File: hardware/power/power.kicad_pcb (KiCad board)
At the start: 2 copper layers, 74 x 34 mm, 18 parts, among them J1 Screw_Terminal_01x02, J2 Screw_Terminal_01x03, Q1 BSS123, U1 AL8861

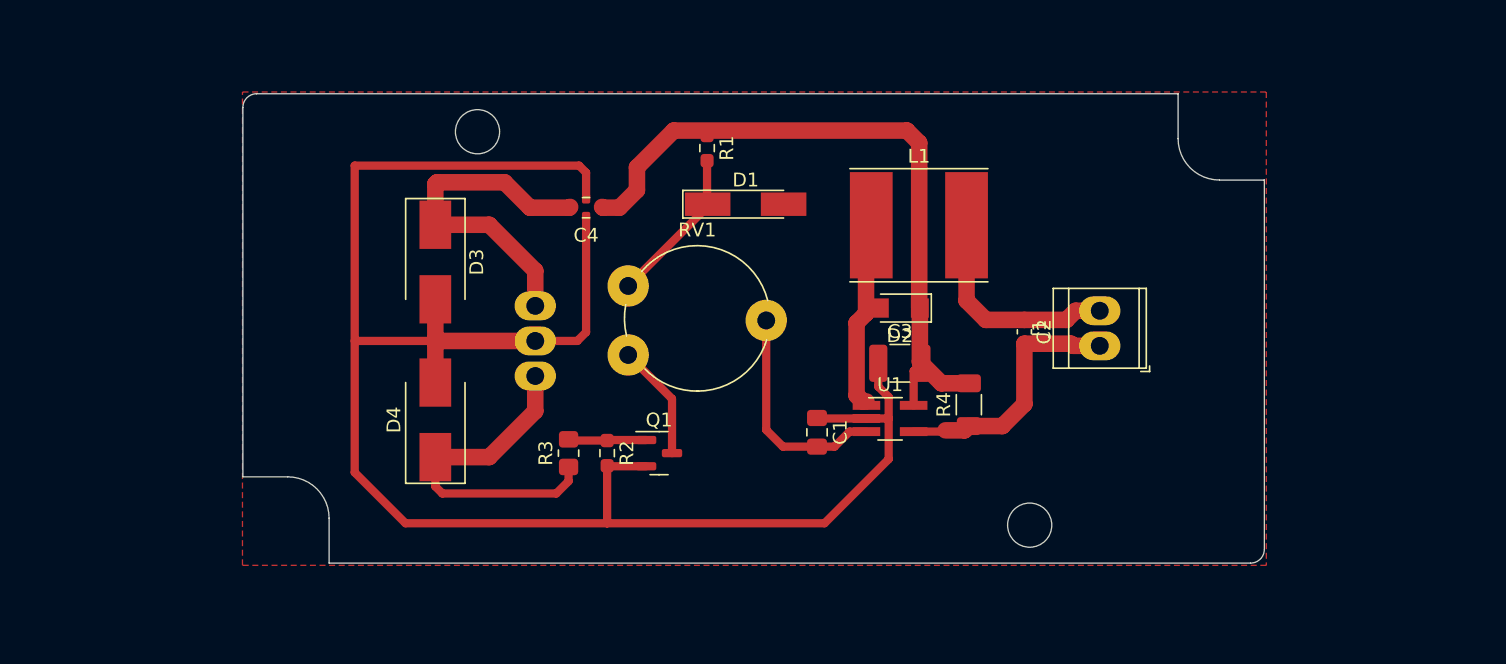
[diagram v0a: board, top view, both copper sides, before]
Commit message: change connectors for SMD ones
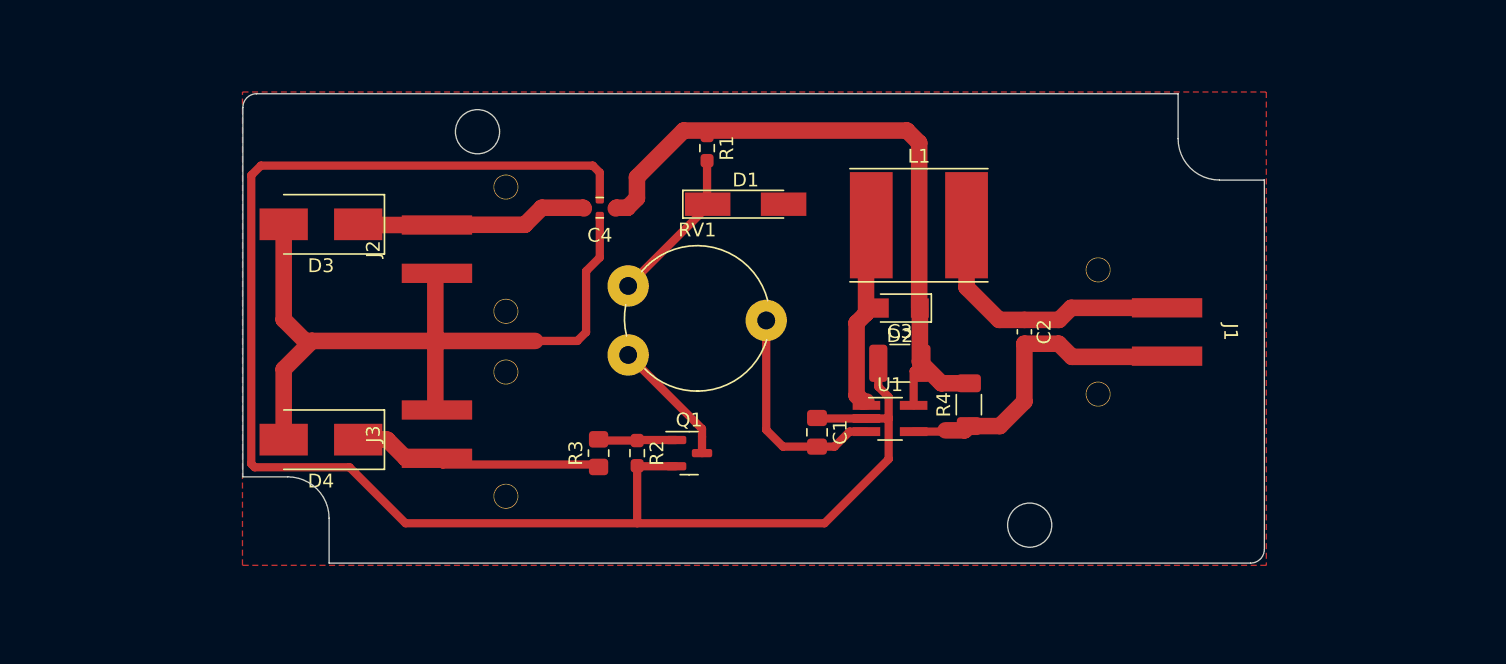
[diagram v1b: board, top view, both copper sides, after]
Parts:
- added J3: Screw_Terminal_01x02, local:amphenol_TZ02, F.Cu at (87.3, 111.4)
- J1: footprint TerminalBlock_TE-Connectivity:TerminalBlock_TE_282834-2_1x02_P2.54mm_Horizontal -> local:amphenol_TZ02
- J2: value Screw_Terminal_01x03 -> Screw_Terminal_01x02; footprint TerminalBlock_TE-Connectivity:TerminalBlock_TE_282834-3_1x03_P2.54mm_Horizontal -> local:amphenol_TZ02; moved to F.Cu
- moved J2 9.32 mm to (87.3, 98.0)
- moved D3 8.73 mm to (70.2, 96.2), turned to 180 degrees
- moved D4 8.41 mm to (70.2, 111.8), turned to 180 degrees
- moved J1 3.95 mm to (122.8, 104.0), turned to -90 degrees
- moved Q1 2.17 mm to (96.9, 112.8)
- moved R2 2.17 mm to (93.1, 112.8)
- moved R3 2.17 mm to (90.3, 112.8)
- moved C4 0.99 mm to (90.4, 95.0)
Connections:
- J1 pad 1: Net-(C2-Pad2) -> Net-(C2-Pad1)
- J1 pad 2: Net-(C2-Pad1) -> Net-(C2-Pad2)
- J2 pad 1: Net-(D4-Pad1) -> GND
- J2 pad 2: GND -> Net-(C4-Pad3)
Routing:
- net GND: track 134.1 -> 174.4 mm
- net Net-(C4-Pad3): track 24.7 -> 16.9 mm
- net Net-(C2-Pad2): track 18.7 -> 23.8 mm
- net Net-(D4-Pad1): track 24.5 -> 19.8 mm
- net Net-(C2-Pad1): track 16.0 -> 20.4 mm
- net +12V: track 49.9 -> 48.9 mm
- net Net-(Q1-Pad3): track 8.43 -> 9.33 mm

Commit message: Add fabrication files
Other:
- board size 74 x 34 mm -> 105 x 44 mm
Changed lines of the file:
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@@
     (pcbplotparams
       (layerselection 0x0000088_7ffffffe)
-      (disableapertmacros true)
+      (disableapertmacros false)
       (usegerberextensions false)
       (usegerberattributes true)
@@
   (gr_line (start 65.541471 86.742043) (end 132.291471 86.742043) (layer "Edge.Cuts") (width 0.09))
   (gr_line (start 138.541471 92.992043) (end 138.541471 119.742043) (layer "Edge.Cuts") (width 0.09))
-  (gr_rect (start 154 126) (end 49 82) (layer "User.1") (width 0.1) (fill none))
+  (gr_rect (start 154 126) (end 49 82) (layer "Edge.Cuts") (width 0.1) (fill none))
   (segment (start 89.408 99.592) (end 89.408 104.013) (width 0.6) (layer "F.Cu") (net 1))
   (segment (start 78.613 104.648) (end 69.552 104.648) (width 1.2) (layer "F.Cu") (net 1))
